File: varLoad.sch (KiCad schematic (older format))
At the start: 7 parts

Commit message: removed voltage divider and second op amp
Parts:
- removed R? (x2): 10k, ~, symbol R
- removed U? (x2): LM741, symbol LM741
- removed VR?: 50k, ~, symbol VR
- added RV?: POT, ~, symbol POT
- added U?: LM324, symbol LM324
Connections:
- net labels added: SOURCE+, SOURCE-
- wire segments 22 -> 17
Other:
- note added: "NEED TO CALCULATE MAX POWER"
- note removed: "Input cct"
- moved on the sheet: R?
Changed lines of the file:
@@
 Sheet 1 1
 Title ""
-Date "24 nov 2013"
+Date "11 feb 2014"
 Rev ""
 Comp ""
@@
 $EndDescr
 $Comp
-L LM741 U?
-U 1 1 526BEDCF
-P 3900 3650
-F 0 "U?" H 4050 3800 60  0000 C CNN
-F 1 "LM741" H 4050 3900 60  0000 C CNN
-F 2 "" H 3900 3650 60  0000 C CNN
-F 3 "" H 3900 3650 60  0000 C CNN
-	1    3900 3650
-	1    0    0    -1
-$EndComp
-$Comp
-L LM741 U?
-U 1 1 526BEDDC
-P 6600 3750
-F 0 "U?" H 6750 3900 60  0000 C CNN
-F 1 "LM741" H 6750 4000 60  0000 C CNN
-F 2 "" H 6600 3750 60  0000 C CNN
-F 3 "" H 6600 3750 60  0000 C CNN
-	1    6600 3750
-	1    0    0    -1
-$EndComp
-$Comp
 L +5V #PWR?
 U 1 1 526BEF9D
-P 3800 2700
-F 0 "#PWR?" H 3800 2790 20  0001 C CNN
-F 1 "+5V" H 3800 2790 30  0000 C CNN
-F 2 "" H 3800 2700 60  0000 C CNN
-F 3 "" H 3800 2700 60  0000 C CNN
-	1    3800 2700
+P 5750 2800
+F 0 "#PWR?" H 5750 2890 20  0001 C CNN
+F 1 "+5V" H 5750 2890 30  0000 C CNN
+F 2 "" H 5750 2800 60  0000 C CNN
+F 3 "" H 5750 2800 60  0000 C CNN
+	1    5750 2800
 	1    0    0    -1
 $EndComp
@@
 L R R?
 U 1 1 526BEFD7
-P 7450 4550
-F 0 "R?" V 7530 4550 40  0000 C CNN
-F 1 "1" V 7457 4551 40  0000 C CNN
-F 2 "~" V 7380 4550 30  0000 C CNN
-F 3 "~" H 7450 4550 30  0000 C CNN
-	1    7450 4550
+P 7450 4850
+F 0 "R?" V 7530 4850 40  0000 C CNN
+F 1 "1" V 7457 4851 40  0000 C CNN
+F 2 "~" V 7380 4850 30  0000 C CNN
+F 3 "~" H 7450 4850 30  0000 C CNN
+	1    7450 4850
 	1    0    0    -1
 $EndComp
@@
 L GND #PWR?
 U 1 1 526BEFFA
-P 7450 4900
-F 0 "#PWR?" H 7450 4900 30  0001 C CNN
-F 1 "GND" H 7450 4830 30  0001 C CNN
-F 2 "" H 7450 4900 60  0000 C CNN
-F 3 "" H 7450 4900 60  0000 C CNN
-	1    7450 4900
-	1    0    0    -1
-$EndComp
-$Comp
-L R R?
-U 1 1 52818700
-P 4850 3650
-F 0 "R?" V 4930 3650 40  0000 C CNN
-F 1 "10k" V 4857 3651 40  0000 C CNN
-F 2 "~" V 4780 3650 30  0000 C CNN
-F 3 "~" H 4850 3650 30  0000 C CNN
-	1    4850 3650
-	0    -1   -1   0
-$EndComp
-$Comp
-L R R?
-U 1 1 5281870D
-P 5150 3900
-F 0 "R?" V 5230 3900 40  0000 C CNN
-F 1 "10k" V 5157 3901 40  0000 C CNN
-F 2 "~" V 5080 3900 30  0000 C CNN
-F 3 "~" H 5150 3900 30  0000 C CNN
-	1    5150 3900
-	-1   0    0    1
-$EndComp
-$Comp
-L GND #PWR?
-U 1 1 52818726
-P 5150 4300
-F 0 "#PWR?" H 5150 4300 30  0001 C CNN
-F 1 "GND" H 5150 4230 30  0001 C CNN
-F 2 "" H 5150 4300 60  0000 C CNN
-F 3 "" H 5150 4300 60  0000 C CNN
-	1    5150 4300
+P 7450 5250
+F 0 "#PWR?" H 7450 5250 30  0001 C CNN
+F 1 "GND" H 7450 5180 30  0001 C CNN
+F 2 "" H 7450 5250 60  0000 C CNN
+F 3 "" H 7450 5250 60  0000 C CNN
+	1    7450 5250
 	1    0    0    -1
 $EndComp
@@
 L GND #PWR?
 U 1 1 52818743
-P 3800 4200
-F 0 "#PWR?" H 3800 4200 30  0001 C CNN
-F 1 "GND" H 3800 4130 30  0001 C CNN
-F 2 "" H 3800 4200 60  0000 C CNN
-F 3 "" H 3800 4200 60  0000 C CNN
-	1    3800 4200
-	1    0    0    -1
-$EndComp
-$Comp
-L VR VR?
-U 1 1 5281876D
-P 2700 3150
-F 0 "VR?" V 2760 3104 40  0000 C TNN
-F 1 "50k" V 2700 3150 40  0000 C CNN
-F 2 "~" H 2700 3150 60  0000 C CNN
-F 3 "~" H 2700 3150 60  0000 C CNN
-	1    2700 3150
+P 5750 4300
+F 0 "#PWR?" H 5750 4300 30  0001 C CNN
+F 1 "GND" H 5750 4230 30  0001 C CNN
+F 2 "" H 5750 4300 60  0000 C CNN
+F 3 "" H 5750 4300 60  0000 C CNN
+	1    5750 4300
 	1    0    0    -1
 $EndComp
@@
 L +5V #PWR?
 U 1 1 528187AC
-P 2700 2700
-F 0 "#PWR?" H 2700 2790 20  0001 C CNN
-F 1 "+5V" H 2700 2790 30  0000 C CNN
-F 2 "" H 2700 2700 60  0000 C CNN
-F 3 "" H 2700 2700 60  0000 C CNN
-	1    2700 2700
+P 4650 2800
+F 0 "#PWR?" H 4650 2890 20  0001 C CNN
+F 1 "+5V" H 4650 2890 30  0000 C CNN
+F 2 "" H 4650 2800 60  0000 C CNN
+F 3 "" H 4650 2800 60  0000 C CNN
+	1    4650 2800
 	1    0    0    -1
 $EndComp
@@
 	1    0    0    -1
 $EndComp
-$Comp
-L +5V #PWR?
-U 1 1 528188C1
-P 6500 2700
-F 0 "#PWR?" H 6500 2790 20  0001 C CNN
-F 1 "+5V" H 6500 2790 30  0000 C CNN
-F 2 "" H 6500 2700 60  0000 C CNN
-F 3 "" H 6500 2700 60  0000 C CNN
-	1    6500 2700
-	1    0    0    -1
-$EndComp
 Wire Wire Line
-	3800 2700 3800 3250
+	5750 2800 5750 3350
 Wire Wire Line
-	7450 4800 7450 4900
+	7450 5100 7450 5250
 Wire Wire Line
-	3400 3750 3100 3750
+	5350 3850 5050 3850
 Wire Wire Line
-	3100 3750 3100 4350
+	5050 3850 5050 4450
 Wire Wire Line
-	3100 4350 4600 4350
+	5050 4450 7450 4450
 Wire Wire Line
-	4600 4350 4600 3650
+	5750 4150 5750 4300
 Wire Wire Line
-	4600 3650 4400 3650
+	4650 2800 4650 3000
 Wire Wire Line
-	5100 3650 6100 3650
+	7450 3950 7450 4600
+Connection ~ 7450 4450
 Wire Wire Line
-	5150 4300 5150 4150
+	6350 3750 7150 3750
 Wire Wire Line
-	3800 4050 3800 4200
-Wire Wire Line
-	2700 3550 3400 3550
-Wire Wire Line
-	2700 3400 2700 3550
-Wire Wire Line
-	2700 2700 2700 2900
-Wire Wire Line
-	7450 3950 7450 4300
-Wire Wire Line
-	7450 4250 6100 4250
-Wire Wire Line
-	6100 4250 6100 3850
-Connection ~ 7450 4250
-Wire Wire Line
-	7100 3750 7150 3750
-Connection ~ 5150 3650
-Wire Wire Line
-	6500 3350 6500 2700
-Wire Wire Line
-	7450 2700 7450 3550
+	7450 2500 7450 3550
 Text Notes 2600 2200 0    60   ~ 0
 Could use USB to power 5V
-Wire Wire Line
-	7450 2700 7750 2700
-Wire Wire Line
-	7800 2900 7600 2900
-Wire Wire Line
-	7600 2900 7600 3200
-$Comp
-L GND #PWR?
-U 1 1 52818BE3
-P 7600 3200
-F 0 "#PWR?" H 7600 3200 30  0001 C CNN
-F 1 "GND" H 7600 3130 30  0001 C CNN
-F 2 "" H 7600 3200 60  0000 C CNN
-F 3 "" H 7600 3200 60  0000 C CNN
-	1    7600 3200
-	1    0    0    -1
-$EndComp
-Text Notes 7850 2800 0    60   ~ 0
-Input cct
-Text Notes 7900 2400 0    60   ~ 0
+Text Notes 7550 2150 0    60   ~ 0
 Design for 30V input & 2Amax
 Text Notes 7700 3750 0    60   ~ 0
@@
 Text Notes 3450 4750 0    60   ~ 0
 LM324\n296-1391-5-ND
+$Comp
+L LM324 U?
+U 1 1 52FA9097
+P 5850 3750
+F 0 "U?" H 5900 3950 60  0000 C CNN
+F 1 "LM324" H 6000 3550 50  0000 C CNN
+F 2 "" H 5850 3750 60  0000 C CNN
+F 3 "" H 5850 3750 60  0000 C CNN
+	1    5850 3750
+	1    0    0    -1
+$EndComp
+$Comp
+L POT RV?
+U 1 1 52FA98D2
+P 4650 3250
+F 0 "RV?" H 4650 3150 50  0000 C CNN
+F 1 "POT" H 4650 3250 50  0000 C CNN
+F 2 "~" H 4650 3250 60  0000 C CNN
+F 3 "~" H 4650 3250 60  0000 C CNN
+	1    4650 3250
+	0    1    1    0
+$EndComp
+Wire Wire Line
+	4800 3250 5000 3250
+Wire Wire Line
+	5000 3250 5000 3650
+Wire Wire Line
+	5000 3650 5350 3650
+$Comp
+L GND #PWR?
+U 1 1 52FA990B
+P 4650 3600
+F 0 "#PWR?" H 4650 3600 30  0001 C CNN
+F 1 "GND" H 4650 3530 30  0001 C CNN
+F 2 "" H 4650 3600 60  0000 C CNN
+F 3 "" H 4650 3600 60  0000 C CNN
+	1    4650 3600
+	1    0    0    -1
+$EndComp
+Wire Wire Line
+	4650 3500 4650 3600
+$Comp
+L GND #PWR?
+U 1 1 52FAAA62
+P 7650 2850
+F 0 "#PWR?" H 7650 2850 30  0001 C CNN
+F 1 "GND" H 7650 2780 30  0001 C CNN
+F 2 "" H 7650 2850 60  0000 C CNN
+F 3 "" H 7650 2850 60  0000 C CNN
+	1    7650 2850
+	1    0    0    -1
+$EndComp
+Wire Wire Line
+	7650 2850 7650 2700
+Wire Wire Line
+	7650 2700 7850 2700
+Wire Wire Line
+	7450 2500 7850 2500
+Text HLabel 7850 2500 2    60   Input ~ 0
+SOURCE+
+Text HLabel 7850 2700 2    60   Input ~ 0
+SOURCE-
+Text Notes 7750 3450 0    60   ~ 0
+NEED TO CALCULATE MAX POWER
 $EndSCHEMATC

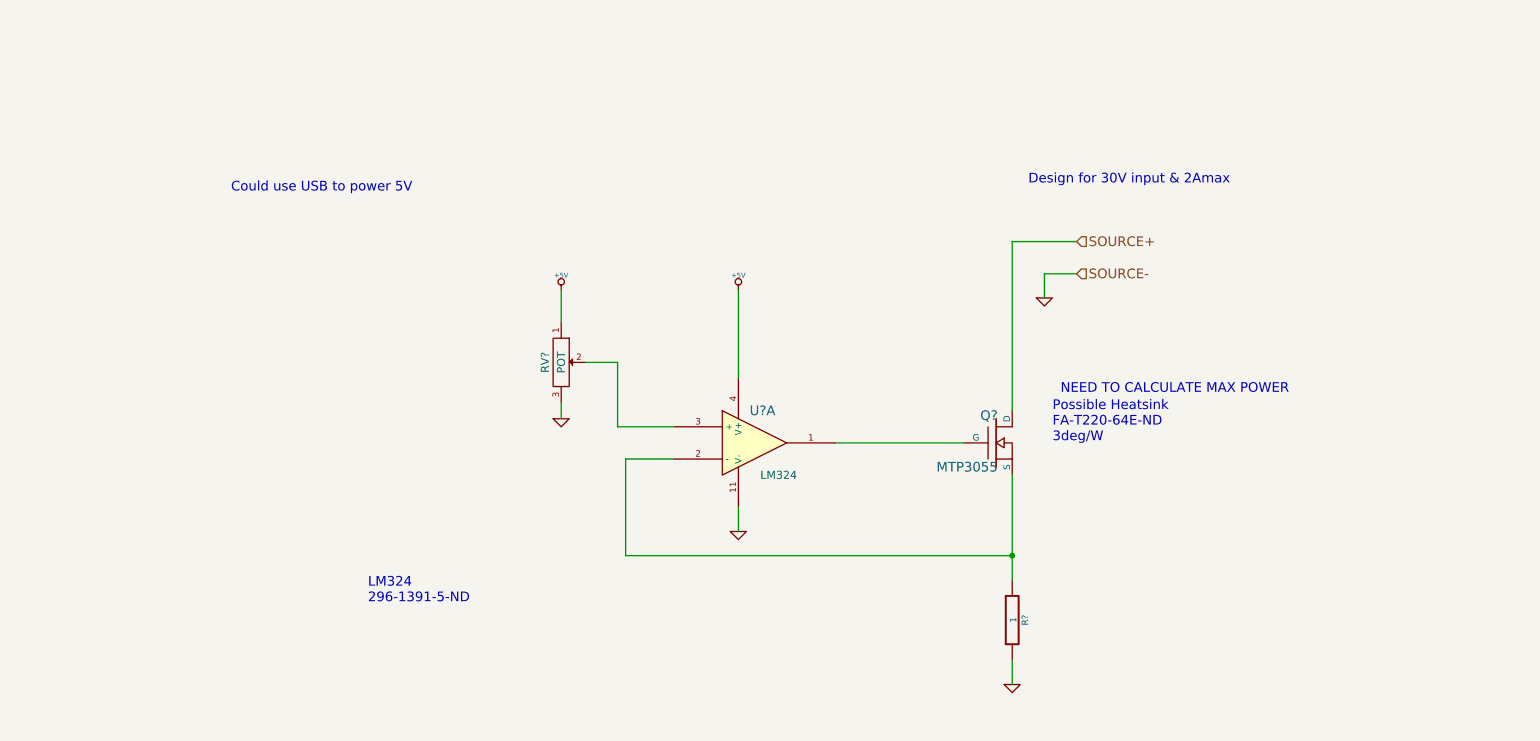
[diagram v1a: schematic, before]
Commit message: Started Associating Footprints.  Re-Added second op amp
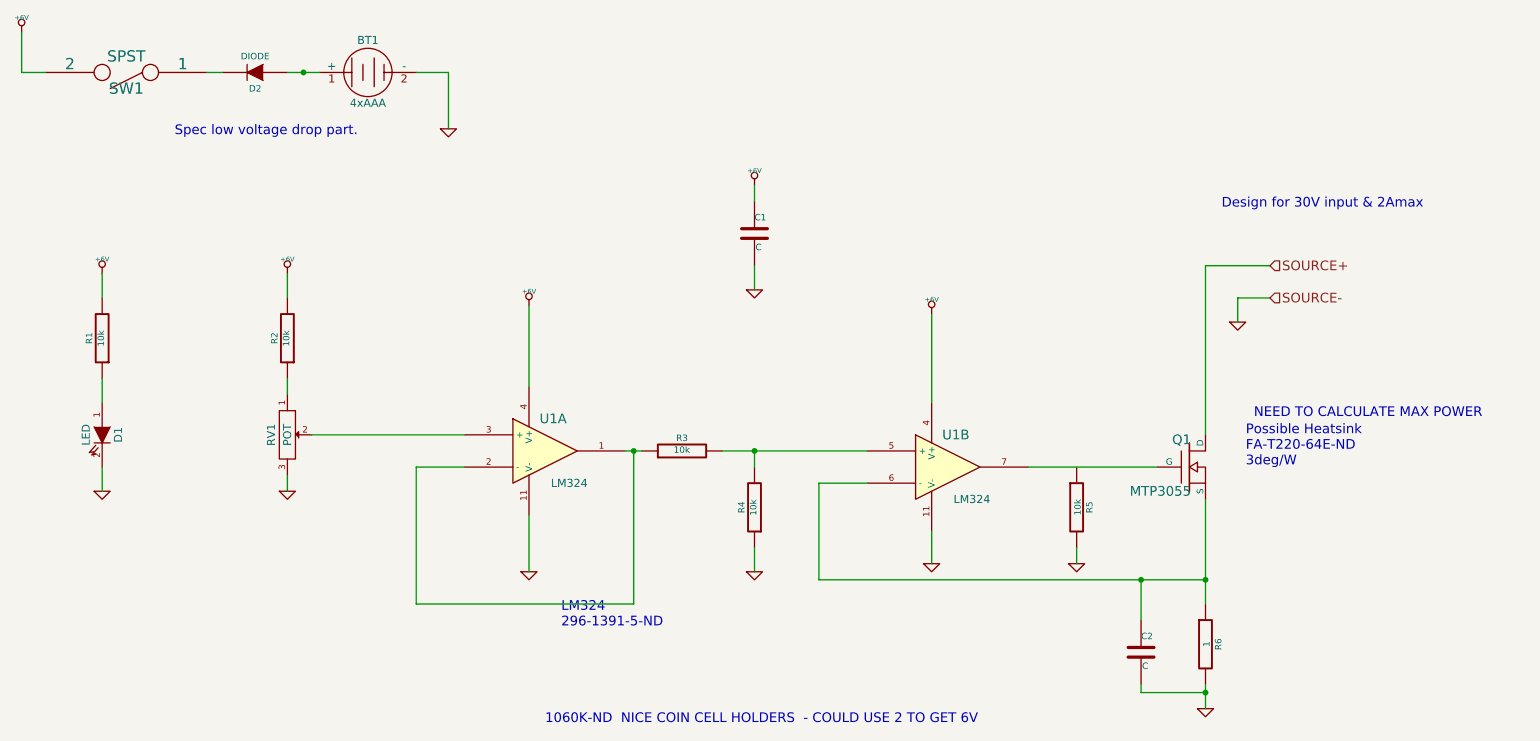
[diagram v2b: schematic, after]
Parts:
- added BT1: 4xAAA, ~, symbol BATTERY
- added C1, C2: C, ~, symbol C
- added D1: LED, ~, symbol LED
- added D2: DIODE, ~, symbol DIODE
- added R1, R2, R3, R4, R5: 10k, ~, symbol R
- added SW1: SPST, ~, symbol SPST
- added unit 1 of U1
- gave numbers to parts that had none: 4
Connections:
- net GND: now also BT1.2 (-), C1.2, C2.2, D1.2 (K), R4.1, R5.2, U1.11 (V-)
- net at Q1.S, R6.1: now also U1.6 (-), C2.1; no longer U1.2 (-)
- net at Q1.G: now also U1.7; no longer U1.1
- net at RV1.2: now also U1.3 (+); no longer U1.3 (+)
- net +5V: no longer names the net of RV1.1
- net +5V: now also R2.1; no longer U1.4 (V+)
- new net: R3.2, R4.2, U1.5 (+)
- new net: R3.1, U1.1, U1.2 (-)
- new net: BT1.1 (+), D2.1 (A)
- new net: D2.2 (K), SW1.1
- new net: D1.1 (A), R1.1
- new net +6V: C1.1, R1.2, R2.2, SW1.2, U1.4 (V+), U1.4 (V+)
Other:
- note added: "1060K-ND NICE COIN CELL HOLDERS - COULD USE 2 TO GET 6V"
- note added: "Spec low voltage drop part."
- note removed: "Could use USB to power 5V"
- moved on the sheet: Q1, R6, RV1
